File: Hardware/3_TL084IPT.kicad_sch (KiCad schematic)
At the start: 23 parts, among them J9 Screw_Terminal_01x08, Q10 N_Mosfet, Q11 N_Mosfet, Q8 N_Mosfet, Q9 N_Mosfet, U13 TL084

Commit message: layout part 2
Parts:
- D16, D17, D18, D19: footprint IVS_FOOTPRINTS:D_MiniMELF -> IVS_FOOTPRINTS:D_SOD323
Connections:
- net VAN10_output: now also R75.2, U13.1; no longer R76.2, U13.7
- net VAN11_output: now also R78.2, U13.14; no longer R77.2, U13.8
- net VAN12_output: now also R77.2, U13.8; no longer R78.2, U13.14
- net VAN9_output: now also R76.2, U13.7; no longer R75.2, U13.1
- net at Q10.2 (S), R69.1: now also U13.12 (+); no longer U13.10 (+)
- net at Q11.2 (S), R70.1: now also U13.10 (+); no longer U13.12 (+)
- net at Q9.2 (S), R68.1: now also U13.3 (+); no longer U13.5 (+)
- net at Q8.2 (S), R67.1: now also U13.5 (+); no longer U13.3 (+)
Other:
- moved on the sheet: C30, R75, R76, R77, R78, U13A, U13B, U13C, U13D, U13E

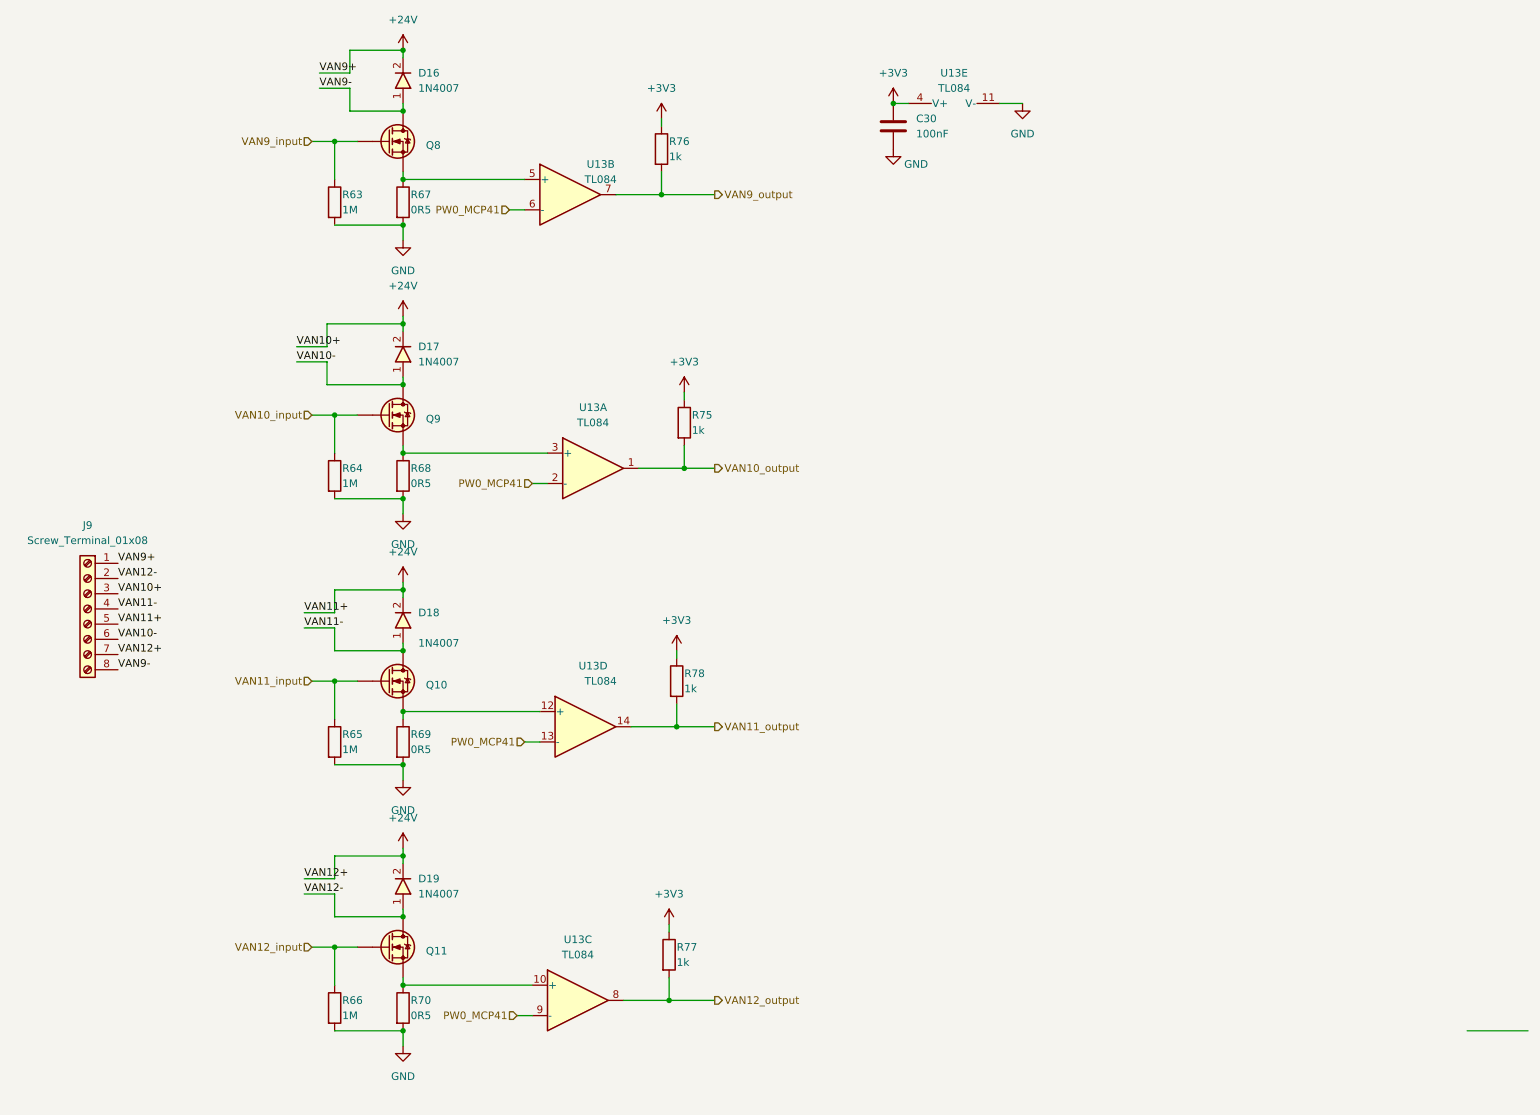
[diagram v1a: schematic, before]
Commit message: add lora, relay, opto, opamp block, led for 74595. Delete RT9193, connect boot0,1 to GND. Fix footprint crystal 8M, 74HC595, IDC pin
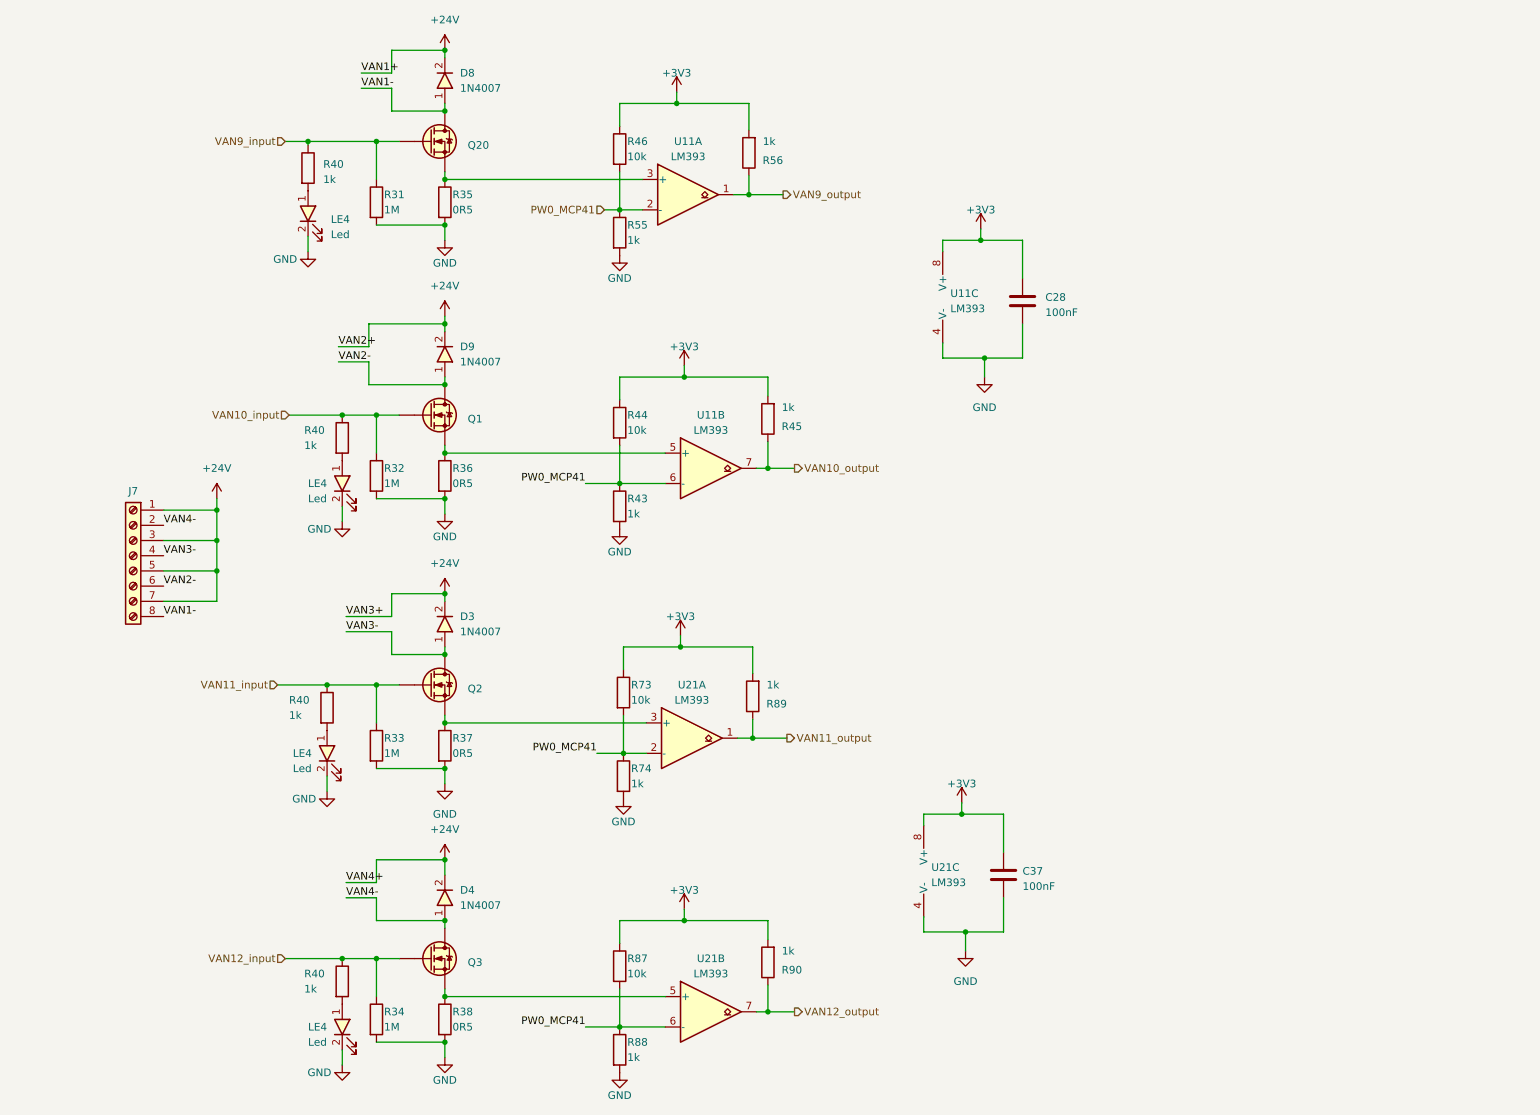
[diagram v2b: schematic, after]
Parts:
- removed C30: 100nF, IVS_FOOTPRINTS:C0603, symbol Device:C
- removed D16, D17, D18, D19: 1N4007, IVS_FOOTPRINTS:D_SOD323, symbol IVS_SYMBOL_DIR:D_Diode
- removed J9: Screw_Terminal_01x08, IVS_FOOTPRINTS:HT-3.96mm, symbol Connector:Screw_Terminal_01x08
- removed Q10, Q11, Q8, Q9: N_Mosfet, IVS_FOOTPRINTS:SOT23-3, symbol IVS_SYMBOLS:N_Mosfet
- removed R63, R64, R65, R66: 1M, IVS_FOOTPRINTS:R0603, symbol Device:R
- removed R67, R68, R69, R70: 0R5, Resistor_SMD:R_0805_2012Metric, symbol Device:R
- removed R75, R76, R77, R78: 1k, IVS_FOOTPRINTS:R0603, symbol Device:R
- removed U13: TL084, IVS_FOOTPRINTS:TSSOP14, symbol Amplifier_Operational:TL084
- added C28, C37: 100nF, IVS_FOOTPRINTS:C_0603, symbol Device:C
- added D3, D4, D8, D9: 1N4007, IVS_FOOTPRINTS:D_SOD323, symbol IVS_SYMBOL_DIR:D_Diode
- added J7: Screw_Terminal_01x08, IVS_FOOTPRINTS:HT-3.96mm, symbol Connector:Screw_Terminal_01x08
- added LE4 (x4): Led, IVS_FOOTPRINTS:LED_0603, symbol IVS_SYMBOLS:Led
- added Q1, Q2, Q20, Q3: N_Mosfet, IVS_FOOTPRINTS:SOT23-3, symbol IVS_SYMBOLS:N_Mosfet
- added R31, R32, R33, R34: 1M, IVS_FOOTPRINTS:R_0603, symbol Device:R
- added R35, R36, R37, R38: 0R5, IVS_FOOTPRINTS:R_0805, symbol Device:R
- added R40 (x4), R43, R45, R55, R56, R74, R88, R89, R90: 1k, IVS_FOOTPRINTS:R_0603, symbol Device:R
- added R44, R46, R73, R87: 10k, IVS_FOOTPRINTS:R_0603, symbol Device:R
- added U11, U21: LM393, IVS_FOOTPRINTS:SOIC-8_3.9x4.9mm_P1.27mm, symbol Comparator:LM393
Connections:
- net +24V: now also D3.2, D4.2, D8.2, D9.2, J7.1 (Pin_1), J7.3 (Pin_3), J7.5 (Pin_5), J7.7 (Pin_7)
- net +3V3: now also C28.1, C37.1, R44.1, R45.2, R46.1, R56.2, R73.1, R87.1, R89.2, R90.2, U11.8 (V+), U21.8 (V+)
- net GND: now also C28.2, C37.2, LE4.2, LE4.2, LE4.2, LE4.2, R31.2, R32.2, R33.2, R34.2, R35.2, R36.2, R37.2, R38.2, R43.2, R55.2, R74.2, R88.2, U11.4 (V-), U21.4 (V-)
- net PW0_MCP41: now also R43.1, R44.2, R46.2, R55.1, R73.2, R74.1, R87.2, R88.1, U11.2 (-), U11.6 (-), U21.2 (-), U21.6 (-)
- net VAN10_input: now also Q1.1 (G), R32.1, R40.1
- net VAN10_output: now also R45.1, U11.7
- net VAN11_input: now also Q2.1 (G), R33.1, R40.1
- net VAN11_output: now also R89.1, U21.1
- net VAN12_input: now also Q3.1 (G), R34.1, R40.1
- net VAN12_output: now also R90.1, U21.7
- net VAN9_input: now also Q20.1 (G), R31.1, R40.1
- net VAN9_output: now also R56.1, U11.1
- new net: Q2.2 (S), R37.1, U21.3 (+)
- new net: Q1.2 (S), R36.1, U11.5 (+)
- new net: LE4.1, R40.2 (x4)
- new net: Q3.2 (S), R38.1, U21.5 (+)
- new net: Q20.2 (S), R35.1, U11.3 (+)
- new net VAN1-: D8.1, J7.8 (Pin_8), Q20.3 (D)
- new net VAN2-: D9.1, J7.6 (Pin_6), Q1.3 (D)
- new net VAN3-: D3.1, J7.4 (Pin_4), Q2.3 (D)
- new net VAN4-: D4.1, J7.2 (Pin_2), Q3.3 (D)
